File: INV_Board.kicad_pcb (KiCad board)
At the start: 2 copper layers, 100 x 50 mm, 170 parts, among them J1 USB_B_Micro, J10 Conn_01x02_Male, J11 Conn_01x04_Male, J12 Conn_01x06_Female, J2 Conn_01x02_Male, J3 Conn_01x02_Male, J4 Conn_01x02_Male, J5 Conn_01x06_Female, J7 Conn_01x03_Male, J8 Conn_ARM_JTAG_SWD_10, J9 Conn_01x06_Male, Q1 Q_NMOS_GDS, Q2 Q_NMOS_GDS, Q3 Q_NMOS_GDS, Q4 Q_NMOS_GDS, Q5 Q_NMOS_GDS, Q6 Q_NMOS_GDS, U2 STM32F303CBTx, U3 IR2181, U4 IR2181, U5 IR2181, U6 TPS76333, U7 LM5017MR, U8 TPS61041DDC, X1 ASE-xxxMHz

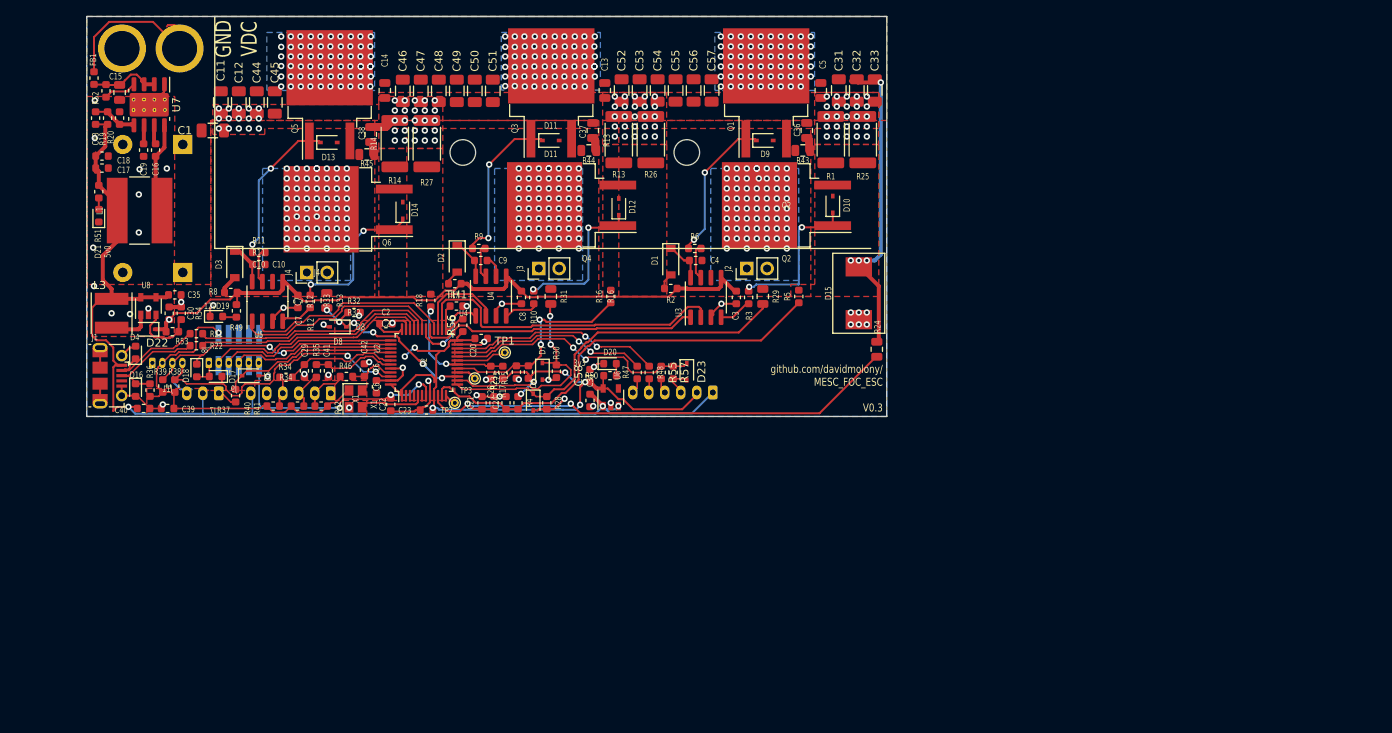
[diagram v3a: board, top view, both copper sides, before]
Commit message: Massive redesign of board to have much bigger power paths (3x the copper and shorter returns) anda 66*84 aspect ratio instead of 50*100. Initial positions for INA181 chips put down.
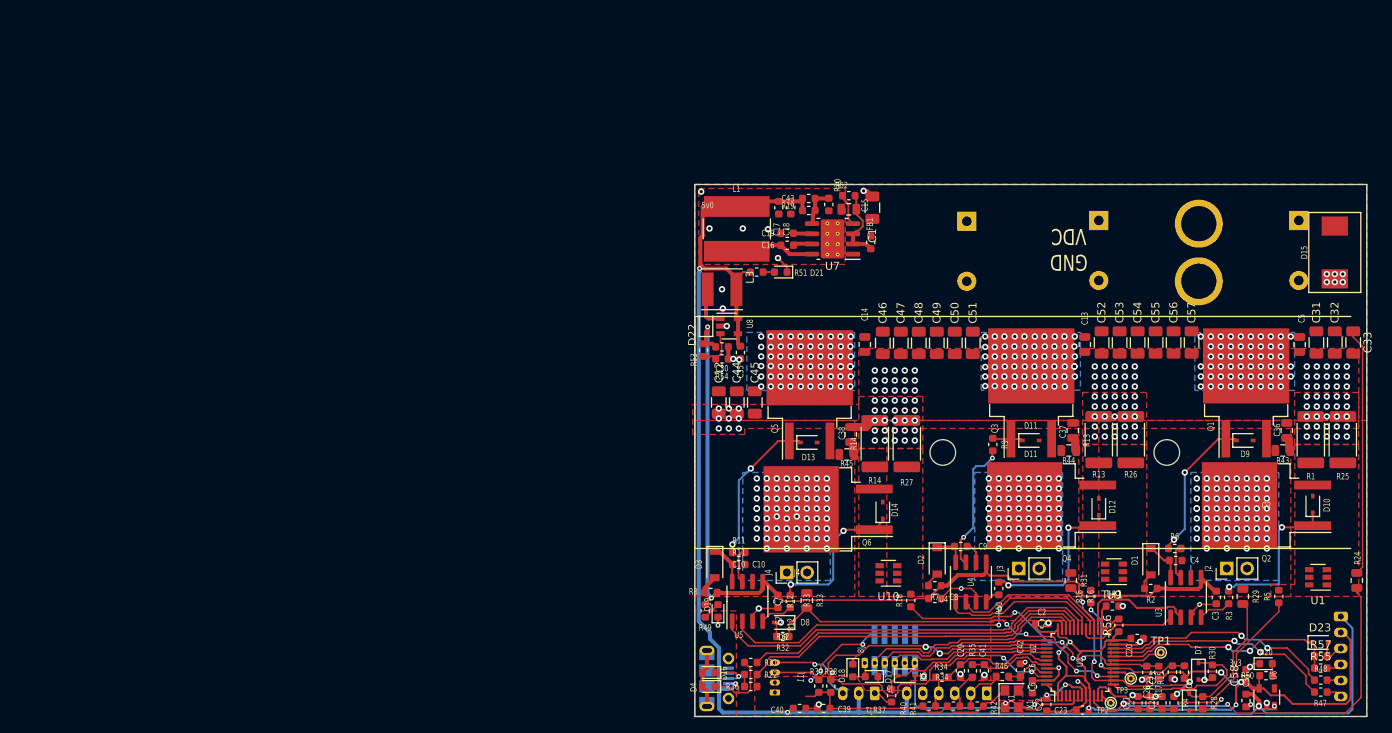
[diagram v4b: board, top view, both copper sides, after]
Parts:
- removed C11: C_1uF 100V, Capacitor_SMD:C_1206_3216Metric
- added C59: CP_470uF+, Capacitor_THT:CP_Radial_D16.0mm_P7.50mm, B.Cu at (191.5, 53.5)
- added U1: INA181, Package_TO_SOT_SMD:SOT-23-6, F.Cu at (193.9, 98.1)
- added U10: INA181, Package_TO_SOT_SMD:SOT-23-6, F.Cu at (140.2, 97.6)
- added U9: INA181, Package_TO_SOT_SMD:SOT-23-6, F.Cu at (168.4, 97.4)
- J1: moved to B.Cu
- moved J10 133.5 mm to (179.0, 57.5), turned to 90 degrees
- moved C27 114.9 mm to (166.5, 53.5), turned to 270 degrees
- moved FB1 99.3 mm to (138.0, 56.2)
- moved C28 98.2 mm to (150.0, 53.6), turned to 270 degrees
- moved R47 94.3 mm to (194.2, 112.5), turned to 0 degrees
- moved R52 93.8 mm to (135.2, 50.4), turned to 0 degrees
- moved R48 92.3 mm to (194.2, 111.0), turned to 180 degrees
- moved C15 92.3 mm to (135.2, 52.1), turned to 180 degrees
- moved R55 90.4 mm to (194.2, 109.5), turned to 0 degrees
- moved C20 90.2 mm to (171.3, 105.8)
- moved C21 90.2 mm to (171.4, 113.8)
- moved C22 90.2 mm to (160.0, 114.0)
- moved C23 90.2 mm to (164.5, 114.7)
- moved C24 90.2 mm to (174.4, 113.8)
- moved C26 90.2 mm to (172.5, 110.0)
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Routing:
- net +5V: track 144.0 -> 202.9 mm, vias 3 -> 4
- net +12V: track 85.2 -> 112.6 mm, vias 1 -> 2
- net +VDC: track 59.5 -> 32.1 mm, vias 185 -> 177
- net ULin: track 40.7 -> 15.4 mm
- net PhaseW: track 22.5 -> 47.4 mm, vias 6 -> 4
- net WLin: track 26.0 -> 50.9 mm, vias 0 -> 2
- net WHin: track 26.1 -> 49.1 mm
- net UHin: track 35.2 -> 12.7 mm
- net ISU_MCU: track 54.0 -> 32.5 mm
- net ISW_MCU: track 15.8 -> 35.5 mm, vias 2 -> 4
- net PhaseU: track 46.6 -> 27.5 mm
- net Net-(D11-Pad1): track 20.1 -> 3.55 mm, vias 2 -> 0
- net /USBDD+: track 29.6 -> 44.1 mm
- net /USBDD-: track 30.4 -> 44.1 mm
- net Net-(R9-Pad1): track 4.40 -> 16.6 mm, vias 0 -> 2
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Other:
- board size 100 x 50 mm -> 84 x 66.5 mm
- board text removed: "12v"

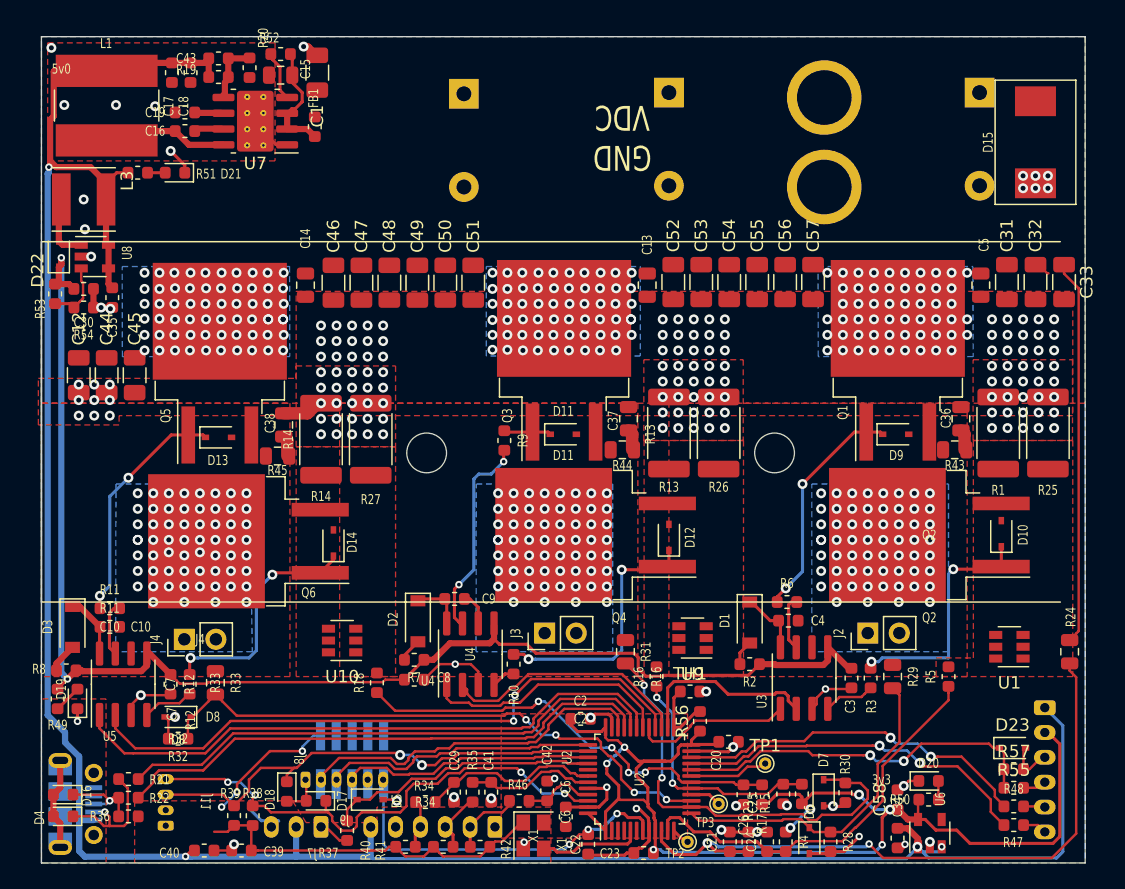
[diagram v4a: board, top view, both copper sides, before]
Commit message: Provisional rearrangement of board to optimise the layout for power paths in light of Zombies comments, and addition of INA181 opamp options.
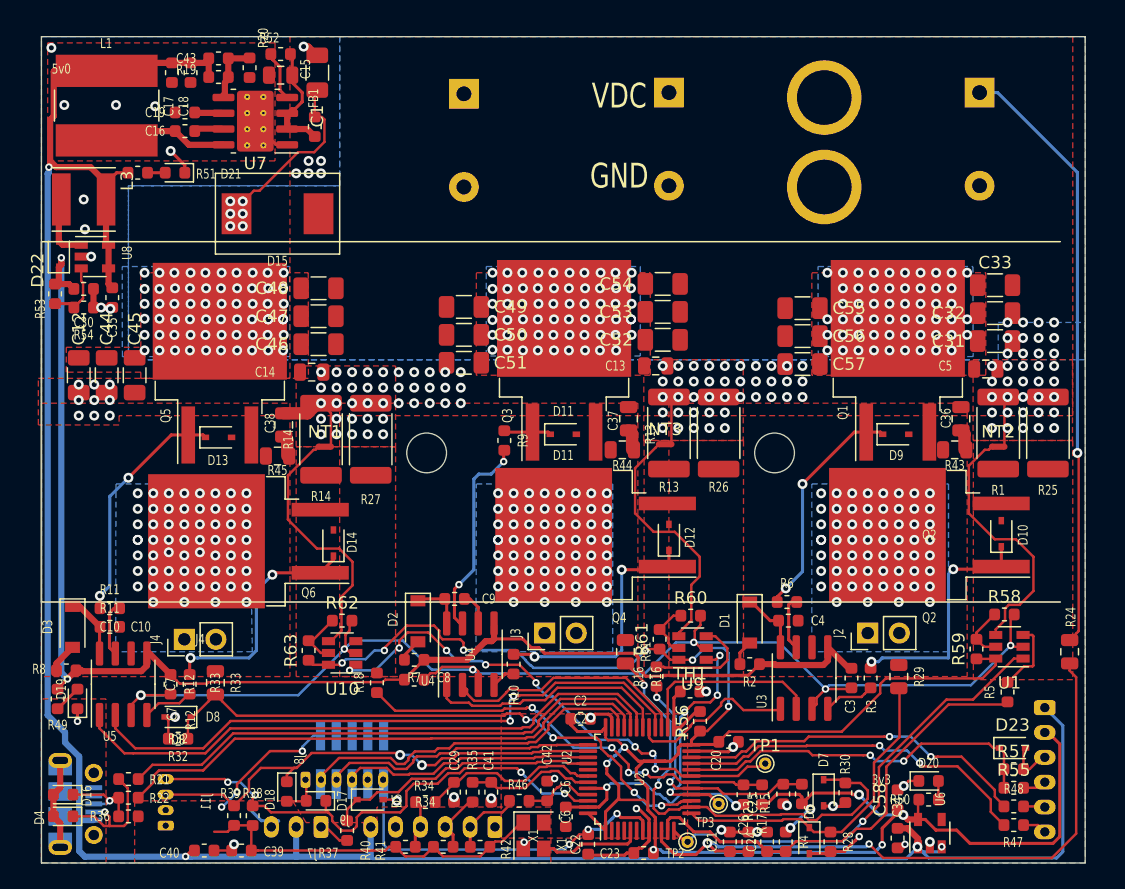
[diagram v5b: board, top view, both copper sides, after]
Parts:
- added NT1: Net-Tie_2, NetTie:NetTie-2_SMD_Pad0.5mm, F.Cu at (138.8, 82.0)
- added NT2: Net-Tie_2, NetTie:NetTie-2_SMD_Pad0.5mm, F.Cu at (193.0, 82.0)
- added NT3: Net-Tie_2, NetTie:NetTie-2_SMD_Pad0.5mm, F.Cu at (166.2, 81.8)
- added R58: R_30k, Resistor_SMD:R_0603_1608Metric, F.Cu at (193.5, 95.5)
- added R59: R_30k, Resistor_SMD:R_0603_1608Metric, F.Cu at (191.2, 98.3)
- added R60: R_30k, Resistor_SMD:R_0603_1608Metric, F.Cu at (168.2, 95.6)
- added R61: R_30k, Resistor_SMD:R_0603_1608Metric, F.Cu at (165.8, 97.5)
- added R62: R_30k, Resistor_SMD:R_0603_1608Metric, F.Cu at (140.2, 96.0)
- added R63: R_30k, Resistor_SMD:R_0603_1608Metric, F.Cu at (137.5, 98.4)
- moved D15 61.3 mm to (135.0, 63.2), turned to 0 degrees
- moved C14 7.02 mm to (137.8, 76.0), turned to 0 degrees
- moved C5 6.76 mm to (192.0, 75.8), turned to 0 degrees
- moved C57 6.65 mm to (177.2, 75.3), turned to 180 degrees
- moved C13 6.54 mm to (165.4, 75.5), turned to 0 degrees
- moved C51 6.49 mm to (150.0, 75.2), turned to 180 degrees
- moved C48 5.72 mm to (138.3, 69.2), turned to 0 degrees
- moved C33 5.56 mm to (192.8, 69.0), turned to 0 degrees
- moved C54 5.35 mm to (166.0, 68.9), turned to 0 degrees
- moved C46 5.09 mm to (138.3, 73.8), turned to 0 degrees
- moved R5 4.91 mm to (193.8, 101.8)
- moved C31 4.84 mm to (192.8, 73.5), turned to 0 degrees
- moved C52 4.73 mm to (166.0, 73.4), turned to 0 degrees
- moved C56 4.57 mm to (177.2, 73.1), turned to 180 degrees
- moved C50 4.46 mm to (150.0, 73.0), turned to 180 degrees
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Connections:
- U1 pad 1: Net-(U1-Pad1) -> /op1Vout
- U1 pad 2: Net-(U1-Pad2) -> GND
- U1 pad 3: Net-(U1-Pad3) -> ISU
- U1 pad 4: Net-(U1-Pad4) -> SGU
- U1 pad 6: Net-(U1-Pad6) -> +3V3
- U10 pad 1: Net-(U10-Pad1) -> /op3Vout
- U10 pad 2: Net-(U10-Pad2) -> GND
- U10 pad 3: Net-(U10-Pad3) -> ISW
- U10 pad 4: Net-(U10-Pad4) -> SGW
- U10 pad 6: Net-(U10-Pad6) -> +3V3
- U9 pad 1: Net-(U9-Pad1) -> /op2Vout
- U9 pad 2: Net-(U9-Pad2) -> GND
- U9 pad 3: Net-(U9-Pad3) -> ISV
- U9 pad 4: Net-(U9-Pad4) -> SGV
- U9 pad 6: Net-(U9-Pad6) -> +3V3
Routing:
- net GND: track 90.8 -> 201.8 mm, vias 171 -> 170
- net +3V3: track 143.5 -> 218.4 mm, vias 11 -> 17
- net /op1Vout: track 1.47 -> 36.9 mm, vias 0 -> 1
- net /op3Vout: track 6.35 -> 41.5 mm, vias 0 -> 8
- net +VDC: track 32.1 -> 63.6 mm, vias 177 -> 184
- net SGU: track 0.00 -> 21.0 mm
- net SGW: track 0.00 -> 20.9 mm
- net SGV: track 0.00 -> 20.1 mm
- net /op2Vout: track 2.65 -> 19.3 mm, vias 0 -> 4
- net ISV: track 0.00 -> 9.05 mm
- net ISU: track 0.00 -> 5.87 mm
- net Net-(R62-Pad1): track 0.00 -> 4.59 mm
- net Net-(R60-Pad1): track 0.00 -> 4.56 mm
- net Net-(R58-Pad1): track 0.00 -> 4.40 mm
- net ISU_MCU: track 32.5 -> 36.6 mm
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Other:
- board text added: "VDC GND"
- board text added: "github.com/davidmolony/ MESC_FOC_ESC V0.4"
- board text removed: "GND VDC"

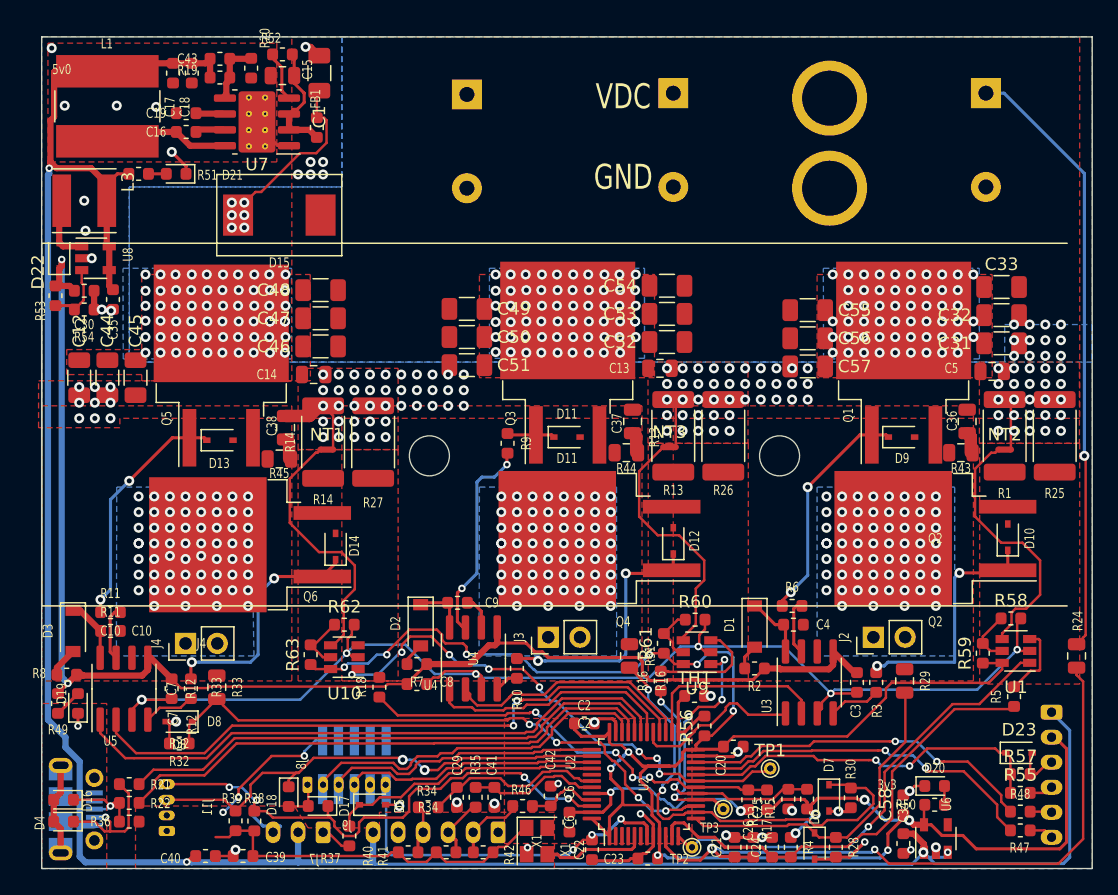
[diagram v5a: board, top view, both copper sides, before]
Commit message: As ordered from JLC PCB 15-12-20, external opamps, rerranged for low impedance ground and Vin and moved DCDC. Added optional input analog on phase voltage wires.
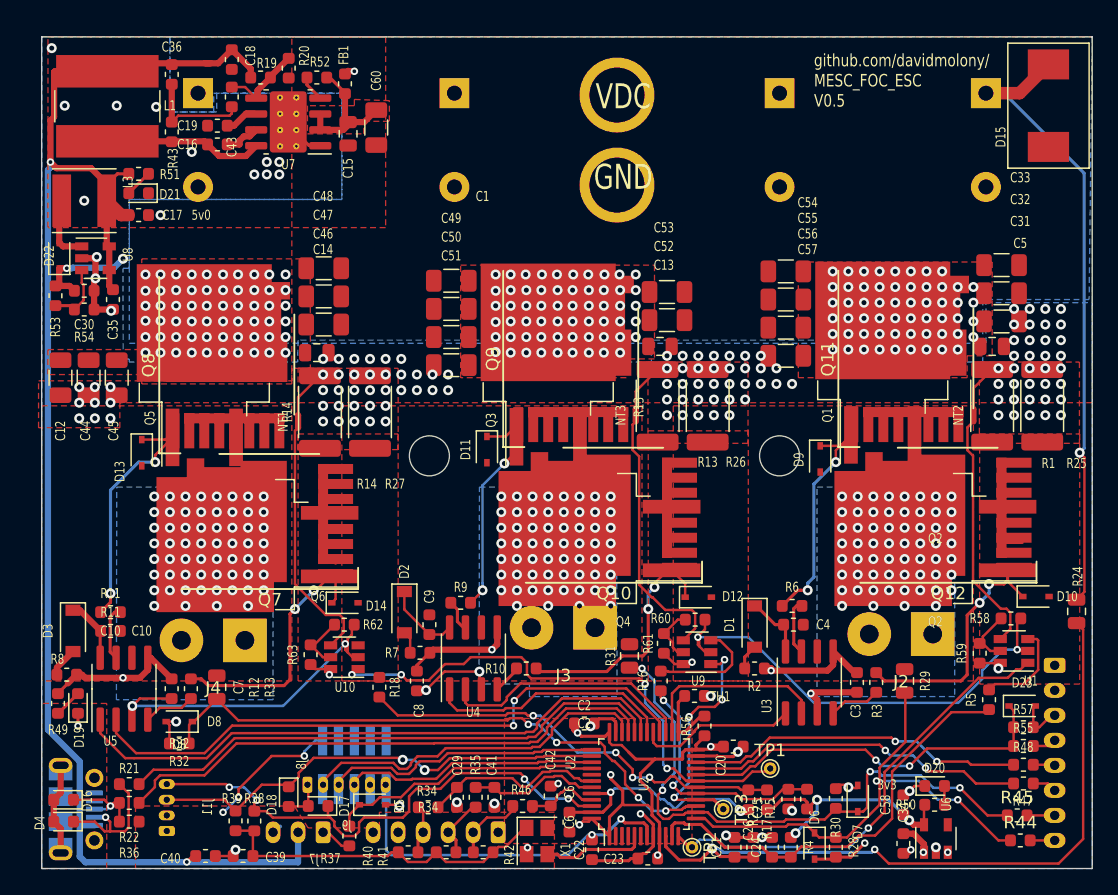
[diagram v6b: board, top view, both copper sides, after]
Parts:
- removed C37, C38: C_0.01uF_100V, Capacitor_SMD:C_0805_2012Metric
- removed J5: Conn_01x06_Female, Connector_JST:JST_PH_B6B-PH-K_1x06_P2.00mm_Vertical
- added C11: CP_470uF+, Capacitor_THT:CP_Radial_D16.0mm_P7.50mm, B.Cu at (128.5, 53.5)
- added C60: C_1uF 100V, Capacitor_SMD:C_1206_3216Metric, F.Cu at (142.8, 56.2)
- added J6: Conn_01x08_Female, Connector_JST:JST_PH_B8B-PH-K_1x08_P2.00mm_Vertical, B.Cu at (197.0, 99.2)
- added Q10: IPT015N10N5, Package_TO_SOT_SMD:Infineon_PG-HSOF-8-1, F.Cu at (161.8, 87.2)
- added Q11: IPT015N10N5, Package_TO_SOT_SMD:Infineon_PG-HSOF-8-1, F.Cu at (185.1, 74.8)
- added Q12: IPT015N10N5, Package_TO_SOT_SMD:Infineon_PG-HSOF-8-1, F.Cu at (188.5, 87.2)
- added Q7: IPT015N10N5, Package_TO_SOT_SMD:Infineon_PG-HSOF-8-1, F.Cu at (134.2, 87.8)
- added Q8: IPT015N10N5, Package_TO_SOT_SMD:Infineon_PG-HSOF-8-1, F.Cu at (130.8, 75.2)
- added Q9: IPT015N10N5, Package_TO_SOT_SMD:Infineon_PG-HSOF-8-1, F.Cu at (158.3, 74.8)
- C16: value C_0.1uF_25V -> C_10nF_16V
- C35: value C_0.1uF_25V -> C_10uF_16V
- C36: value C_0.01uF_100V -> C_3nF_16V; footprint Capacitor_SMD:C_0805_2012Metric -> Capacitor_SMD:C_0603_1608Metric
- C43: value C_100pF_16V -> C_10nF_16V
- J2, J3, J4: footprint Connector_PinHeader_2.54mm:PinHeader_1x02_P2.54mm_Vertical -> Connector_Wire:SolderWirePad_1x02_P5.08mm_Drill1.5mm
- L1: value L_120uH_1.0A -> L_150uH_1.0A
- R1, R13, R14, R25, R26, R27: value R_Shunt_2mR -> R_Shunt_1mR
- R43: value R_1 -> R_100k; footprint Resistor_SMD:R_0805_2012Metric -> Resistor_SMD:R_0603_1608Metric
- R44, R45: value R_1 -> R_1k5; footprint Resistor_SMD:R_0805_2012Metric -> Resistor_SMD:R_0603_1608Metric
- R52: value R_30k -> R_100k
- moved C36 69.4 mm to (126.4, 52.0)
- moved R43 68.1 mm to (126.4, 56.6), turned to 270 degrees
- moved R45 65.5 mm to (194.0, 111.2), turned to 0 degrees
- moved D15 62.1 mm to (196.5, 54.5), turned to 270 degrees
- moved R44 44.2 mm to (194.2, 113.2), turned to 0 degrees
- moved C1 19.7 mm to (148.8, 68.5), turned to 180 degrees
- moved J10 17.0 mm to (162.0, 57.2)
- moved R9 13.3 mm to (149.5, 94.2), turned to 0 degrees
- moved C17 11.7 mm to (123.8, 63.2), turned to 0 degrees
- moved C54 9.57 mm to (175.5, 67.8), turned to 180 degrees
- moved C27 8.50 mm to (175.0, 53.5)
- moved C15 7.01 mm to (140.5, 56.8), turned to 270 degrees
- moved D9 6.73 mm to (178.2, 82.8), turned to 270 degrees
- moved D11 6.48 mm to (151.6, 82.0), turned to 270 degrees
- moved D13 6.33 mm to (124.0, 82.2), turned to 270 degrees
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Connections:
- net Net-(D10-Pad1) renamed /UGL
- net Net-(D11-Pad1) renamed /VGH
- net Net-(D12-Pad1) renamed /VGL
- net Net-(D13-Pad1) renamed /WGH
- net Net-(D14-Pad1) renamed /WGL
- net Net-(D9-Pad1) renamed /UGH
- C36 pad 1: GND -> +5V
- C43 pad 1: +5V -> Net-(C36-Pad2)
- R43 pad 2: SWU -> Net-(C16-Pad2)
- R44 pad 1: Net-(C37-Pad2) -> PhaseU
- R44 pad 2: SWV -> Net-(J6-Pad8)
- R45 pad 1: Net-(C38-Pad2) -> PhaseV
- R45 pad 2: SWW -> Net-(J6-Pad7)
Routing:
- net +3V3: track 218.4 -> 105.4 mm, vias 17 -> 14
- net +5V: track 202.9 -> 128.7 mm
- net GND: track 201.8 -> 170.7 mm, vias 170 -> 158
- net /VGH: track 3.55 -> 17.8 mm, vias 0 -> 2
- net Net-(R9-Pad1): track 16.6 -> 2.63 mm, vias 2 -> 0
- net +12V: track 112.6 -> 126.0 mm, vias 2 -> 5
- net PhaseU: track 26.3 -> 39.4 mm, vias 0 -> 2
- net +VDC: track 63.6 -> 51.6 mm, vias 184 -> 178
- net PhaseV: track 37.2 -> 47.4 mm, vias 2 -> 4
- net Net-(C36-Pad2): track 1.68 -> 8.65 mm
- net ISU: track 5.87 -> 9.53 mm
- net Vsense_MCU: track 54.4 -> 58.0 mm
- net Net-(C16-Pad2): track 11.4 -> 13.9 mm
- net /WGH: track 19.2 -> 21.5 mm
- net Net-(J6-Pad7): track 0.00 -> 2.21 mm
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- added copper zone on In2.Cu, net +12V
- added copper zone on In2.Cu, net +3V3
- added copper zone on In2.Cu, net +5V
- added copper zone on In2.Cu, net +VDC
- added copper zone on In1.Cu, net GND
- added copper zone on F.Cu, net Net-(C15-Pad1)
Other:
- copper layers 2 -> 4
- board text added: "5V 3V3 G An Rx Tx An An"
- board text added: "github.com/davidmolony/ MESC_FOC_ESC V0.5"
- board text removed: "5V 3V3 G An Rx Tx"
- board text removed: "github.com/davidmolony/ MESC_FOC_ESC V0.3"
- board text removed: "github.com/davidmolony/ MESC_FOC_ESC V0.4"
